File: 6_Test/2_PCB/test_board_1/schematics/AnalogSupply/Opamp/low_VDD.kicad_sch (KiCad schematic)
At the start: 4 parts, among them U1 ADA4807-1AKSZ-R7

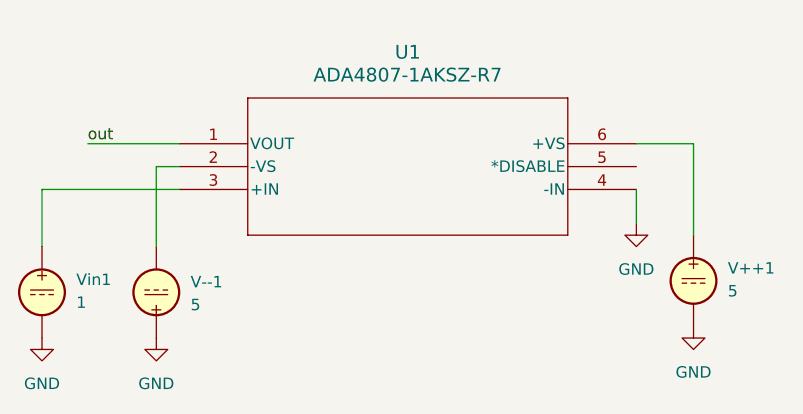
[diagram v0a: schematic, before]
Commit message: progress on op amp. ldo done
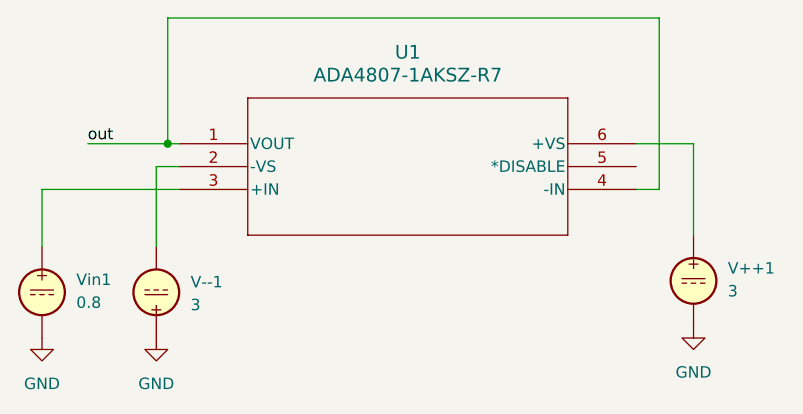
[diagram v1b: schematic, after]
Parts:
- V++1, V--1: value 5 -> 3
- Vin1: value 1 -> 0.8
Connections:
- net GND: no longer U1.4 (-IN)
- net out: now also U1.4 (-IN)
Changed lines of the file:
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@@
 	(generator_version "8.0")
 	(paper "A4")
+	(junction
+		(at 125.73 104.14)
+		(diameter 0)
+		(color 0 0 0 0)
+	)
 	(wire
 		(pts
@@
 	(wire
 		(pts
+			(xy 180.34 109.22) (xy 177.8 109.22)
+		)
+		(stroke
+			(width 0)
+			(type default)
+		)
+	)
+	(wire
+		(pts
+			(xy 180.34 90.17) (xy 180.34 109.22)
+		)
+		(stroke
+			(width 0)
+			(type default)
+		)
+	)
+	(wire
+		(pts
 			(xy 124.46 106.68) (xy 127 106.68)
 		)
@@
 	(wire
 		(pts
+			(xy 125.73 104.14) (xy 125.73 90.17)
+		)
+		(stroke
+			(width 0)
+			(type default)
+		)
+	)
+	(wire
+		(pts
 			(xy 184.15 104.14) (xy 184.15 114.3)
 		)
@@
 	(wire
 		(pts
-			(xy 116.84 104.14) (xy 127 104.14)
+			(xy 116.84 104.14) (xy 125.73 104.14)
 		)
 		(stroke
@@
 	(wire
 		(pts
-			(xy 177.8 113.03) (xy 177.8 109.22)
-		)
-		(stroke
-			(width 0)
-			(type default)
-		)
-	)
-	(wire
-		(pts
 			(xy 111.76 109.22) (xy 111.76 115.57)
+		)
+		(stroke
+			(width 0)
+			(type default)
+		)
+	)
+	(wire
+		(pts
+			(xy 125.73 104.14) (xy 127 104.14)
+		)
+		(stroke
+			(width 0)
+			(type default)
+		)
+	)
+	(wire
+		(pts
+			(xy 125.73 90.17) (xy 180.34 90.17)
 		)
 		(stroke
@@
 			)
 		)
-		(property "Value" "5"
+		(property "Value" "3"
 			(at 187.96 120.5201 0)
 			(effects
@@
 			)
 		)
-		(property "Value" "5"
+		(property "Value" "3"
 			(at 128.27 122.0497 0)
 			(effects
@@
 				(path "/95e5dcee-77e4-4cc3-9d7c-d0dc3cd96a78"
 					(reference "V--1")
-					(unit 1)
-				)
-			)
-		)
-	)
-	(symbol
-		(lib_id "power:GND")
-		(at 177.8 113.03 0)
-		(unit 1)
-		(exclude_from_sim no)
-		(in_bom yes)
-		(on_board yes)
-		(dnp no)
-		(fields_autoplaced yes)
-		(property "Reference" "#PWR03"
-			(at 177.8 119.38 0)
-			(effects
-				(font
-					(size 1.27 1.27)
-				)
-				(hide yes)
-			)
-		)
-		(property "Value" "GND"
-			(at 177.8 118.11 0)
-			(effects
-				(font
-					(size 1.27 1.27)
-				)
-			)
-		)
-		(property "Footprint" ""
-			(at 177.8 113.03 0)
-			(effects
-				(font
-					(size 1.27 1.27)
-				)
-				(hide yes)
-			)
-		)
-		(property "Datasheet" ""
-			(at 177.8 113.03 0)
-			(effects
-				(font
-					(size 1.27 1.27)
-				)
-				(hide yes)
-			)
-		)
-		(property "Description" "Power symbol creates a global label with name \"GND\" , ground"
-			(at 177.8 113.03 0)
-			(effects
-				(font
-					(size 1.27 1.27)
-				)
-				(hide yes)
-			)
-		)
-		(pin "1"
-		)
-		(instances
-			(project ""
-				(path "/95e5dcee-77e4-4cc3-9d7c-d0dc3cd96a78"
-					(reference "#PWR03")
 					(unit 1)
 				)
@@
 			)
 		)
-		(property "Value" "1"
+		(property "Value" "0.8"
 			(at 115.57 121.7901 0)
 			(effects
